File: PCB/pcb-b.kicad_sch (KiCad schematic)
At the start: 11 parts, among them U1 L7805, U2 L7805, U3 L7805

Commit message: fixes
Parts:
- added GND-1, GND-2: ~, Connector_Wire:SolderWire-1.5sqmm_1x03_P6mm_D1.7mm_OD3mm, symbol Connector_Generic:Conn_01x03
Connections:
- net GND: now also GND-1.1 (Pin_1), GND-1.2 (Pin_2), GND-1.3 (Pin_3), GND-2.1 (Pin_1), GND-2.2 (Pin_2), GND-2.3 (Pin_3)

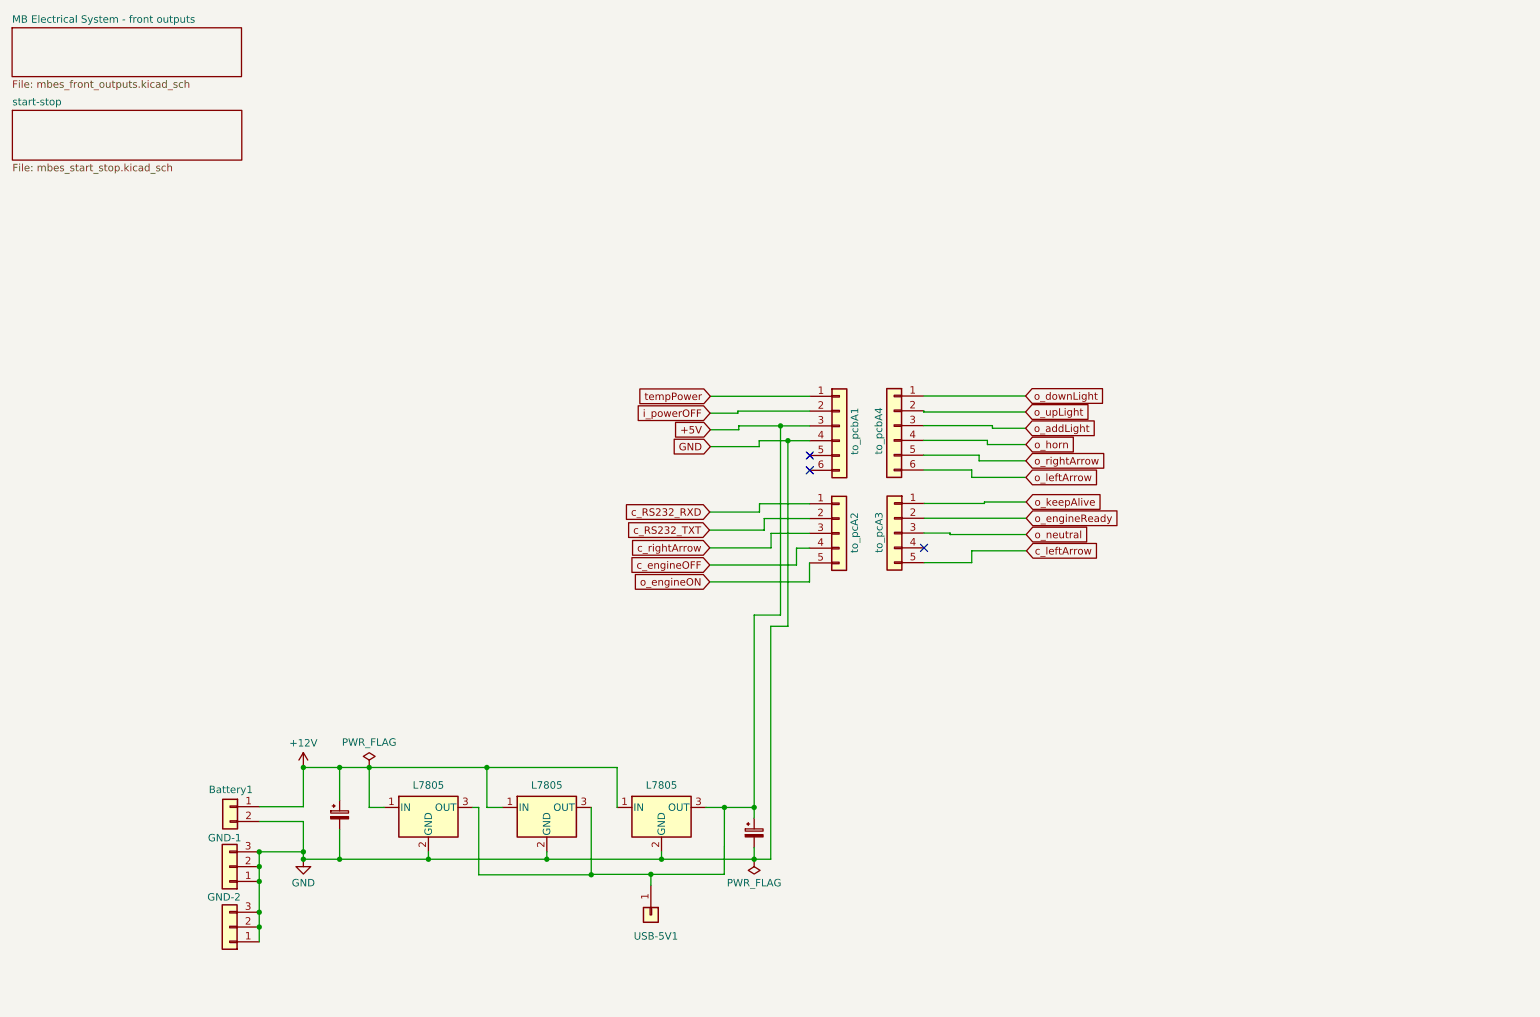
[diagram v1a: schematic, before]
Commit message: Many changes
- The power drivers component has been implemented with TPCA8120 P-ch MOSfet
- The temp-power management has been moved from pcb-a to pcb-b
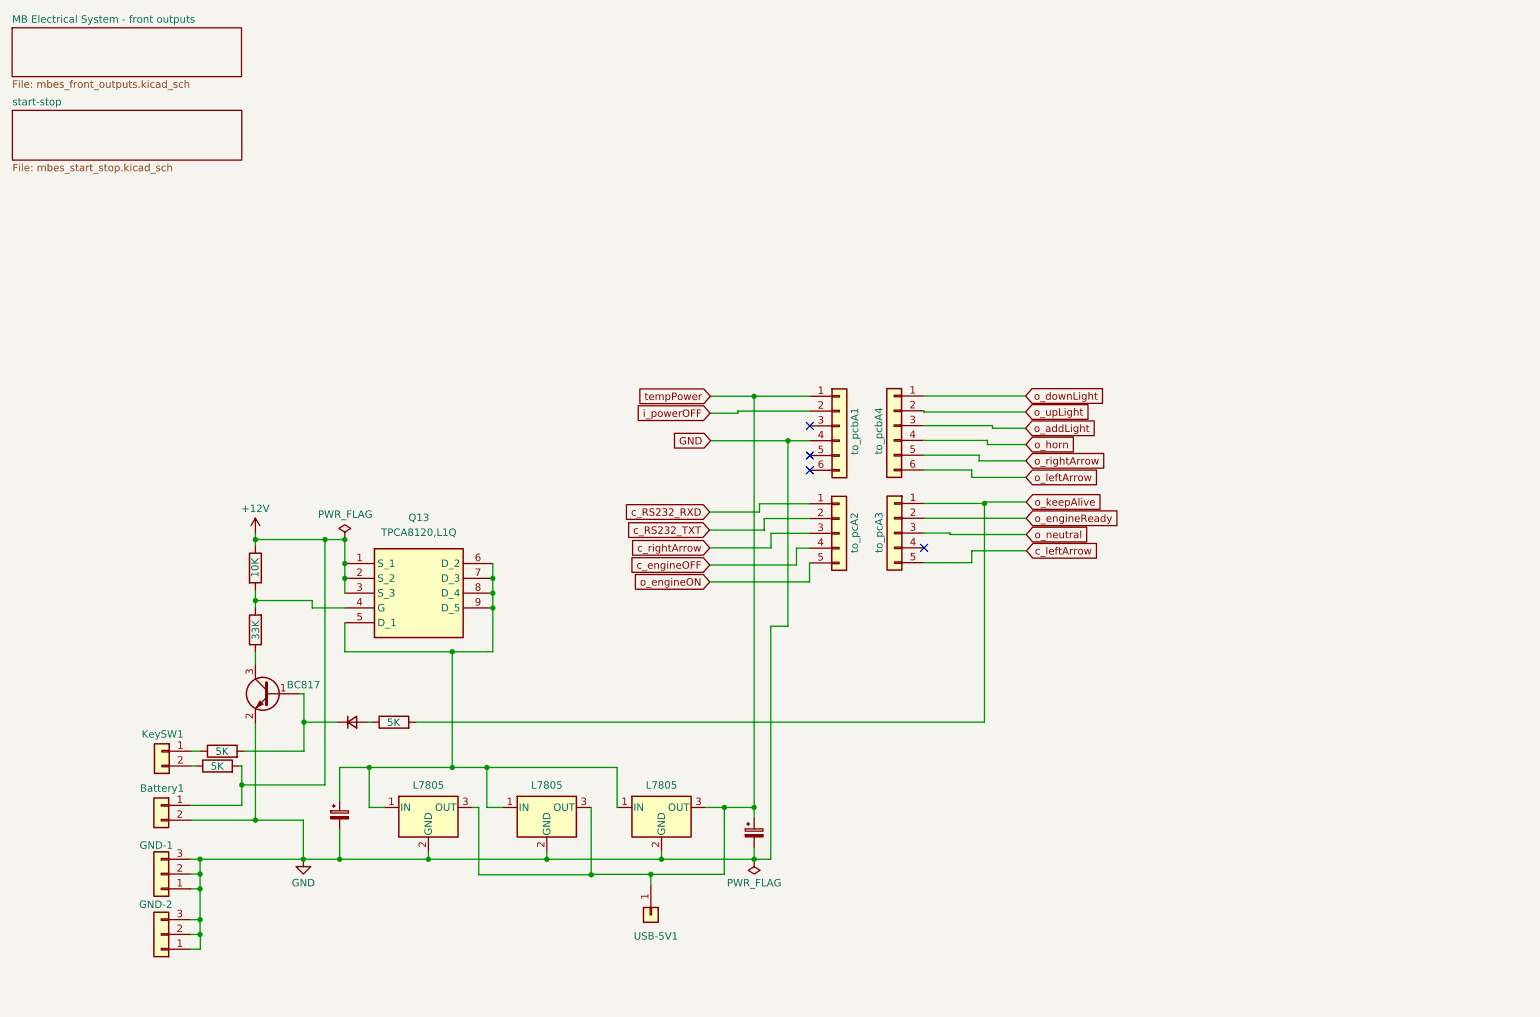
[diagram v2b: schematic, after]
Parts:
- added D1: D_Small, Diode_SMD:D_1210_3225Metric_Pad1.42x2.65mm_HandSolder, symbol Device:D_Small
- added KeySW1: Conn_01x02, Connector_PinHeader_2.54mm:PinHeader_1x02_P2.54mm_Vertical, symbol Connector_Generic:Conn_01x02
- added Q13: TPCA8120,L1Q, TPCA8120:TPH4R003NLL1Q, symbol TPCA8120-L1Q:TPCA8120,L1Q
- added Q9: BC817, Package_TO_SOT_SMD:SOT-23, symbol Transistor_BJT:BC817
- added R1, R4, R5: 5K, Resistor_SMD:R_1206_3216Metric, symbol Device:R
- added R2: 10K, Resistor_SMD:R_1206_3216Metric, symbol Device:R
- added R3: 33K, Resistor_SMD:R_1206_3216Metric, symbol Device:R
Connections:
- net +12V: now also Q13.1 (S_1), Q13.2 (S_2), Q13.3 (S_3), R1.2, R2.1; no longer C9.1, U1.1 (IN), U2.1 (IN), U3.1 (IN)
- net GND: now also Q9.2 (E)
- net o_keepAlive: now also R5.2
- net tempPower: now also C1.1, U1.3 (OUT), U2.3 (OUT), U3.3 (OUT), USB-5V1.1 (Pin_1)
- removed net +5V: C1.1, U1.3 (OUT), U2.3 (OUT), U3.3 (OUT), USB-5V1.1 (Pin_1), to_pcbA1.3 (Pin_3)
- new net: KeySW1.2 (Pin_2), R1.1
- new net: C9.1, Q13.5 (D_1), Q13.6 (D_2), Q13.7 (D_3), Q13.8 (D_4), Q13.9 (D_5), U1.1 (IN), U2.1 (IN), U3.1 (IN)
- new net: Q13.4 (G), R2.2, R3.2
- new net: D1.1 (K), Q9.1 (B), R4.2
- new net: Q9.3 (C), R3.1
- new net: KeySW1.1 (Pin_1), R4.1
- new net: D1.2 (A), R5.1
- no-connect marks 3 -> 4
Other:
- moved on the sheet: Battery1, GND-1, GND-2

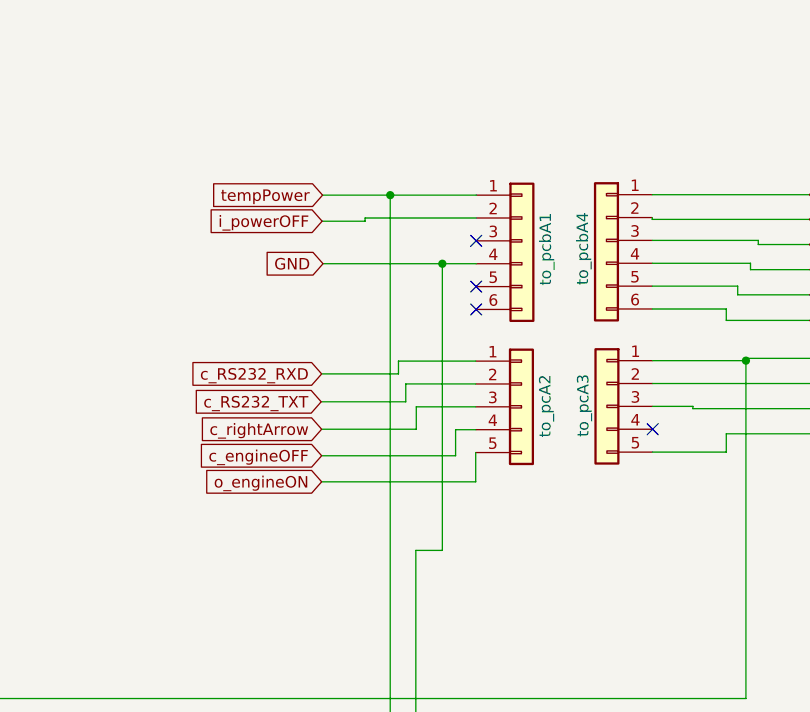
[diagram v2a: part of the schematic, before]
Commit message: Changes and enhancements
- File porting to Kicad-8
- SSR has been replaced by Mosfet deplation N-Channel
- "to-PCB-a-1" connector has been changed with tree pins one
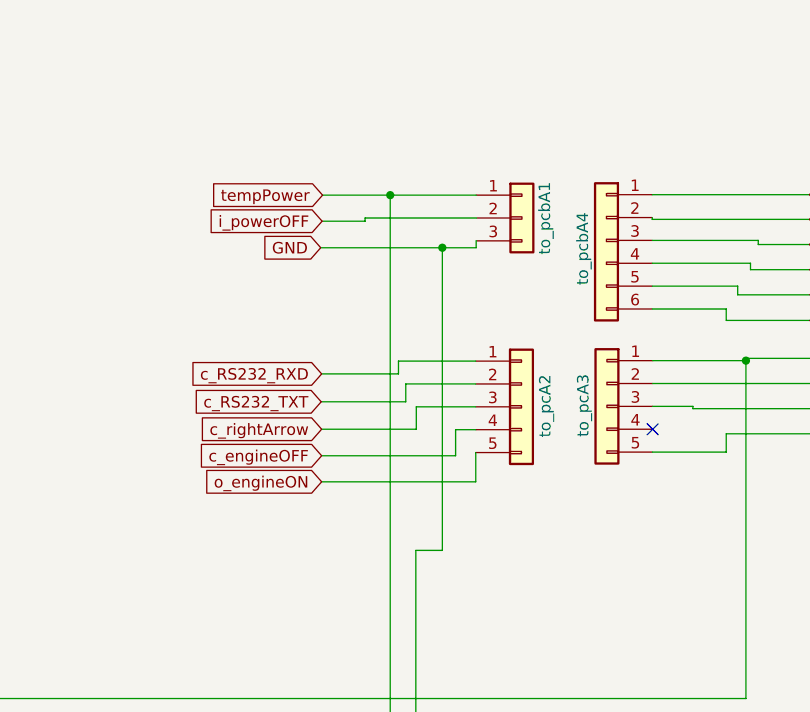
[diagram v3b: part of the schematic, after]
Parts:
- removed to_pcbA1: Conn_01x06, Connector_PinSocket_2.54mm:PinSocket_1x06_P2.54mm_Vertical, symbol Connector_Generic:Conn_01x06
- added to_pcbA1: Conn_01x03, Connector_PinSocket_2.54mm:PinSocket_1x03_P2.54mm_Vertical, symbol Connector_Generic:Conn_01x03
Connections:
- net GND: now also to_pcbA1.3 (Pin_3)
- net i_powerOFF: now also to_pcbA1.2 (Pin_2)
- net tempPower: now also to_pcbA1.1 (Pin_1)
- no-connect marks 4 -> 1

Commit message: Size reducing and component rationalization
- RS232(TTL) lines on PCB-B have been removed (MAX232 is already mounted in PCB-A)
- The two PCB can no more be connected using pin-header connectors. You have to use welded wires, now.
  (this solution is not beautiful as the original, but it is a more flexible one and it also allowd me
  to reduce the PCB size)

The PCBs size is approximately 109.7mm x 43.5mm.
For this dual-face sigle-layer (THT) version this is the minimum size I can achieve.
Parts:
- removed to_pcA2: Conn_01x05, Connector_PinSocket_2.54mm:PinSocket_1x05_P2.54mm_Vertical, symbol Connector_Generic:Conn_01x05
- added to_pcA2: Conn_01x03, Connector_PinSocket_2.54mm:PinSocket_1x03_P2.54mm_Vertical, symbol Connector_Generic:Conn_01x03
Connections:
- net c_engineOFF: now also to_pcA2.2 (Pin_2)
- net c_rightArrow: now also to_pcA2.1 (Pin_1)
- net o_engineON: now also to_pcA2.3 (Pin_3)
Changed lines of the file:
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@@
+	(wire
+		(pts
+			(xy 150.114 111.0996) (xy 133.35 111.0996)
+		)
+		(stroke
+			(width 0)
+			(type default)
+		)
+	)
 	(wire
 		(pts
@@
 	(wire
 		(pts
-			(xy 150.3172 111.3536) (xy 150.3172 108.1024)
+			(xy 150.114 107.95) (xy 150.114 111.0996)
 		)
 		(stroke
@@
 	(wire
 		(pts
-			(xy 133.1976 99.3648) (xy 141.732 99.3648)
-		)
-		(stroke
-			(width 0)
-			(type default)
-		)
-	)
-	(wire
-		(pts
 			(xy 146.6088 118.9736) (xy 143.6624 118.9736)
 		)
@@
 	(wire
 		(pts
-			(xy 141.732 97.9424) (xy 150.3172 97.9424)
-		)
-		(stroke
-			(width 0)
-			(type default)
-		)
-	)
-	(wire
-		(pts
 			(xy 89.0016 143.2052) (xy 94.9452 143.2052)
 		)
@@
 	(wire
 		(pts
+			(xy 150.114 107.95) (xy 150.368 107.95)
+		)
+		(stroke
+			(width 0)
+			(type default)
+		)
+	)
+	(wire
+		(pts
 			(xy 93.5482 150.0632) (xy 92.5322 150.0632)
 		)
@@
 	(wire
 		(pts
-			(xy 143.7132 105.5116) (xy 143.7132 103.0224)
+			(xy 143.764 105.2576) (xy 143.764 102.87)
 		)
 		(stroke
@@
 	(wire
 		(pts
-			(xy 142.5448 102.4636) (xy 142.5448 100.4824)
-		)
-		(stroke
-			(width 0)
-			(type default)
-		)
-	)
-	(wire
-		(pts
 			(xy 55.2196 104.0892) (xy 55.2196 105.156)
 		)
@@
 	(wire
 		(pts
-			(xy 141.732 99.3648) (xy 141.732 97.9424)
-		)
-		(stroke
-			(width 0)
-			(type default)
-		)
-	)
-	(wire
-		(pts
 			(xy 44.1452 152.2476) (xy 55.2196 152.2476)
 		)
@@
 	(wire
 		(pts
-			(xy 142.5448 100.4824) (xy 150.3172 100.4824)
-		)
-		(stroke
-			(width 0)
-			(type default)
-		)
-	)
-	(wire
-		(pts
 			(xy 89.0016 123.3424) (xy 95.9612 123.3424)
 		)
@@
 	(wire
 		(pts
-			(xy 133.1976 105.5116) (xy 143.7132 105.5116)
+			(xy 133.35 105.2576) (xy 143.764 105.2576)
 		)
 		(stroke
@@
 	(wire
 		(pts
-			(xy 133.1468 102.4636) (xy 142.5448 102.4636)
-		)
-		(stroke
-			(width 0)
-			(type default)
-		)
-	)
-	(wire
-		(pts
 			(xy 69.2912 135.4328) (xy 63.5508 135.4328)
 		)
@@
 	(wire
 		(pts
-			(xy 133.1976 111.3536) (xy 150.3172 111.3536)
-		)
-		(stroke
-			(width 0)
-			(type default)
-		)
-	)
-	(wire
-		(pts
 			(xy 52.8828 146.2024) (xy 52.8828 142.9512)
 		)
@@
 	(wire
 		(pts
-			(xy 148.082 108.458) (xy 148.082 105.5624)
+			(xy 148.1328 108.204) (xy 148.1328 105.41)
 		)
 		(stroke
@@
 	(wire
 		(pts
-			(xy 148.082 105.5624) (xy 150.3172 105.5624)
+			(xy 148.1328 105.41) (xy 150.368 105.41)
 		)
 		(stroke
@@
 	(wire
 		(pts
-			(xy 133.1976 108.458) (xy 148.082 108.458)
+			(xy 133.35 108.204) (xy 148.1328 108.204)
 		)
 		(stroke
@@
 	(wire
 		(pts
-			(xy 143.7132 103.0224) (xy 150.3172 103.0224)
+			(xy 143.764 102.87) (xy 150.368 102.87)
 		)
 		(stroke
@@
 		)
 	)
-	(global_label "c_RS232_RXD"
+	(global_label "c_rightArrow"
 		(shape input)
-		(at 133.1976 99.3648 180)
+		(at 133.35 105.2576 180)
 		(fields_autoplaced yes)
 		(effects
@@
 		)
 		(property "Intersheetrefs" "${INTERSHEET_REFS}"
-			(at 133.1976 99.3648 0)
+			(at 133.35 105.2576 0)
 			(effects
 				(font
@@
 		)
 		(property "Riferimenti inter-foglio" "${INTERSHEET_REFS}"
-			(at 117.9031 99.2854 0)
-			(effects
-				(font
-					(size 1.27 1.27)
-				)
-				(justify right)
-				(hide yes)
-			)
-		)
-	)
-	(global_label "c_rightArrow"
-		(shape input)
-		(at 133.1976 105.5116 180)
-		(fields_autoplaced yes)
-		(effects
-			(font
-				(size 1.27 1.27)
-			)
-			(justify right)
-		)
-		(property "Intersheetrefs" "${INTERSHEET_REFS}"
-			(at 133.1976 105.5116 0)
-			(effects
-				(font
-					(size 1.27 1.27)
-				)
-				(hide yes)
-			)
-		)
-		(property "Riferimenti inter-foglio" "${INTERSHEET_REFS}"
-			(at 119.1731 105.591 0)
+			(at 119.3255 105.337 0)
 			(effects
 				(font
@@
 	(global_label "c_engineOFF"
 		(shape input)
-		(at 133.1976 108.458 180)
+		(at 133.35 108.204 180)
 		(fields_autoplaced yes)
 		(effects
@@
 		)
 		(property "Intersheetrefs" "${INTERSHEET_REFS}"
-			(at 133.1976 108.458 0)
+			(at 133.35 108.204 0)
 			(effects
 				(font
@@
 		)
 		(property "Riferimenti inter-foglio" "${INTERSHEET_REFS}"
-			(at 118.9916 108.5374 0)
+			(at 119.144 108.2834 0)
 			(effects
 				(font
@@
 		)
 	)
-	(global_label "c_RS232_TXT"
-		(shape input)
-		(at 133.1468 102.4636 180)
-		(fields_autoplaced yes)
-		(effects
-			(font
-				(size 1.27 1.27)
-			)
-			(justify right)
-		)
-		(property "Intersheetrefs" "${INTERSHEET_REFS}"
-			(at 133.1468 102.4636 0)
-			(effects
-				(font
-					(size 1.27 1.27)
-				)
-				(hide yes)
-			)
-		)
-		(property "Riferimenti inter-foglio" "${INTERSHEET_REFS}"
-			(at 118.457 102.3842 0)
-			(effects
-				(font
-					(size 1.27 1.27)
-				)
-				(justify right)
-				(hide yes)
-			)
-		)
-	)
 	(global_label "o_downLight"
 		(shape input)
@@
 	(global_label "o_engineON"
 		(shape input)
-		(at 133.1976 111.3536 180)
+		(at 133.35 111.0996 180)
 		(fields_autoplaced yes)
 		(effects
@@
 		)
 		(property "Intersheetrefs" "${INTERSHEET_REFS}"
-			(at 133.1976 111.3536 0)
+			(at 133.35 111.0996 0)
 			(effects
 				(font
@@
 		)
 		(property "Riferimenti inter-foglio" "${INTERSHEET_REFS}"
-			(at 119.7778 111.2742 0)
+			(at 119.9302 111.0202 0)
 			(effects
 				(font
@@
 	(symbol
 		(lib_id "Connector_Generic:Conn_01x03")
+		(at 155.448 105.41 0)
+		(unit 1)
+		(exclude_from_sim no)
+		(in_bom yes)
+		(on_board yes)
+		(dnp no)
+		(property "Reference" "to_pcA2"
+			(at 157.734 108.712 90)
+			(effects
+				(font
+					(size 1.27 1.27)
+				)
+				(justify left)
+			)
+		)
+		(property "Value" "Conn_01x03"
+			(at 158.242 106.6799 0)
+			(effects
+				(font
+					(size 1.27 1.27)
+				)
+				(justify left)
+				(hide yes)
+			)
+		)
+		(property "Footprint" "Connector_PinSocket_2.54mm:PinSocket_1x03_P2.54mm_Vertical"
+			(at 155.448 105.41 0)
+			(effects
+				(font
+					(size 1.27 1.27)
+				)
+				(hide yes)
+			)
+		)
+		(property "Datasheet" "~"
+			(at 155.448 105.41 0)
+			(effects
+				(font
+					(size 1.27 1.27)
+				)
+				(hide yes)
+			)
+		)
+		(property "Description" "Generic connector, single row, 01x03, script generated (kicad-library-utils/schlib/autogen/connector/)"
+			(at 155.448 105.41 0)
+			(effects
+				(font
+					(size 1.27 1.27)
+				)
+				(hide yes)
+			)
+		)
+		(pin "3"
+		)
+		(pin "2"
+		)
+		(pin "1"
+		)
+		(instances
+			(project ""
+				(path "/709d0967-afe5-49d3-92a5-d2bb94550bdb"
+					(reference "to_pcA2")
+					(unit 1)
+				)
+			)
+		)
+	)
+	(symbol
+		(lib_id "Connector_Generic:Conn_01x03")
 		(at 39.0652 161.4932 180)
 		(unit 1)
@@
 					(unit 1)
 				)
-			)
-		)
-	)
-	(symbol
-		(lib_id "Connector_Generic:Conn_01x05")
-		(at 155.3972 103.0224 0)
-		(unit 1)
-		(exclude_from_sim no)
-		(in_bom yes)
-		(on_board yes)
-		(dnp no)
-		(property "Reference" "to_pcA2"
-			(at 158.0388 102.9208 90)
-			(effects
-				(font
-					(size 1.27 1.27)
-				)
-			)
-		)
-		(property "Value" "Conn_01x05"
-			(at 155.3972 94.1324 0)
-			(effects
-				(font
-					(size 1.27 1.27)
-				)
-				(hide yes)
-			)
-		)
-		(property "Footprint" "Connector_PinSocket_2.54mm:PinSocket_1x05_P2.54mm_Vertical"
-			(at 155.3972 103.0224 0)
-			(effects
-				(font
-					(size 1.27 1.27)
-				)
-				(hide yes)
-			)
-		)
-		(property "Datasheet" "~"
-			(at 155.3972 103.0224 0)
-			(effects
-				(font
-					(size 1.27 1.27)
-				)
-				(hide yes)
-			)
-		)
-		(property "Description" ""
-			(at 155.3972 103.0224 0)
-			(effects
-				(font
-					(size 1.27 1.27)
-				)
-				(hide yes)
-			)
-		)
-		(pin "1"
-		)
-		(pin "2"
-		)
-		(pin "3"
-		)
-		(pin "4"
-		)
-		(pin "5"
-		)
-		(instances
-			(project "pcb-b"
-				(path "/709d0967-afe5-49d3-92a5-d2bb94550bdb"
-					(reference "to_pcA2")
-					(unit 1)
-				)
